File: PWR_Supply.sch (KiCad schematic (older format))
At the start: 0 parts

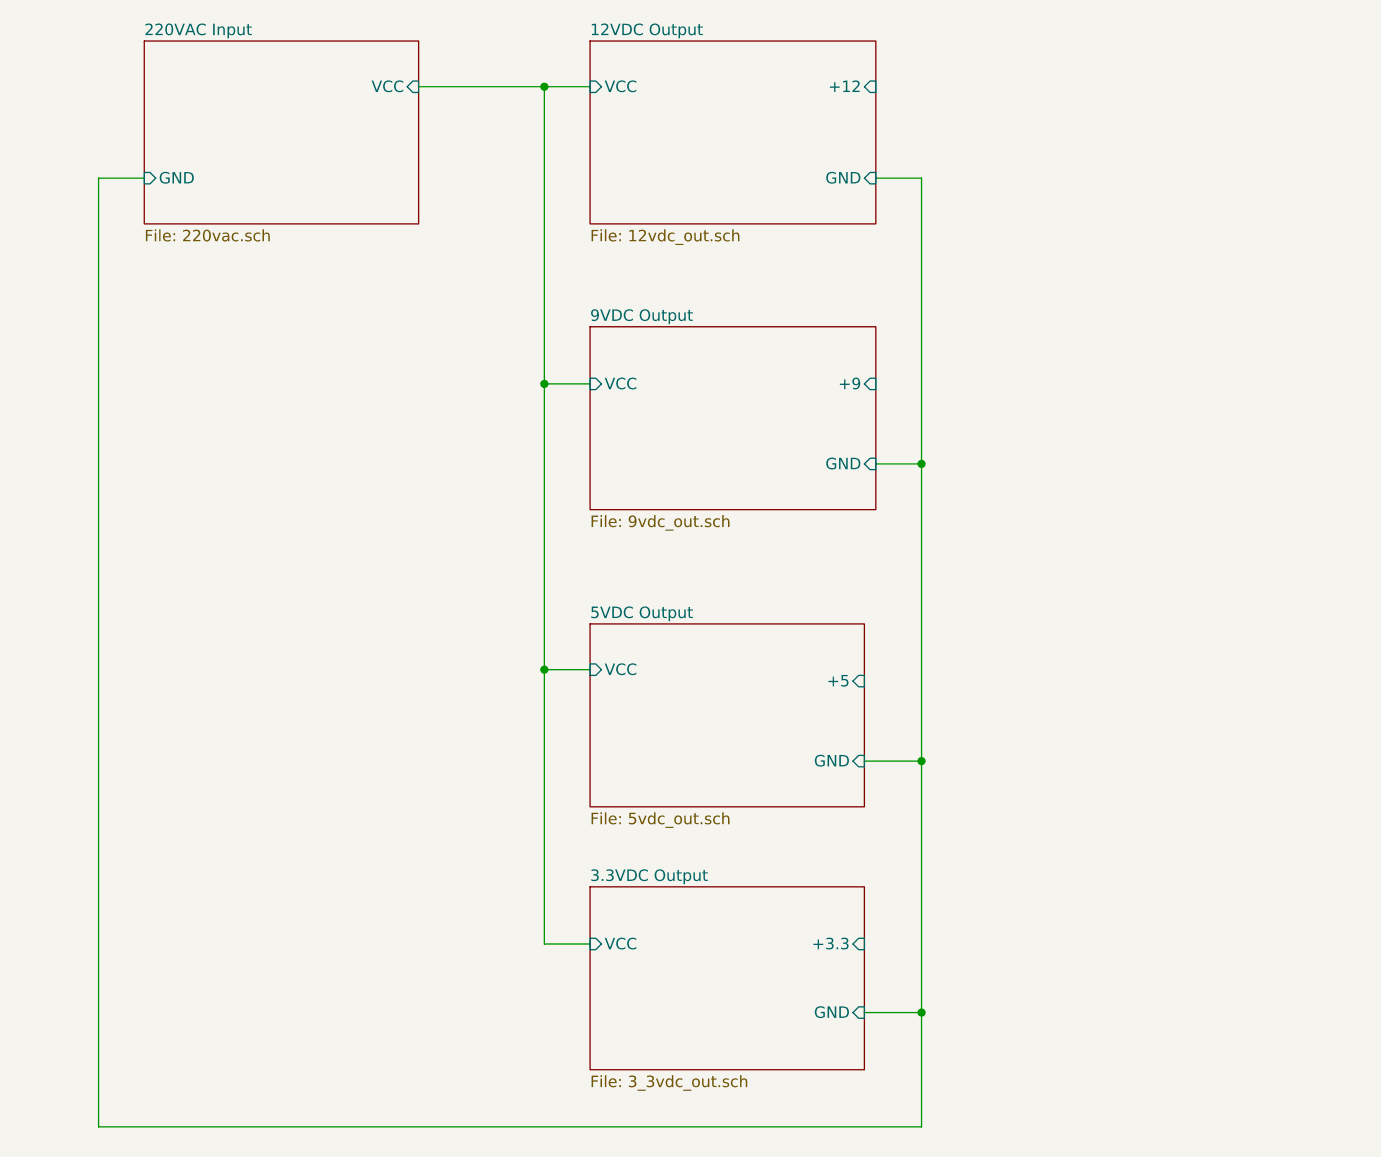
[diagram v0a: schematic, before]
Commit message: Fixed ERC errors, combined all outputs into a bus, fixed annotations
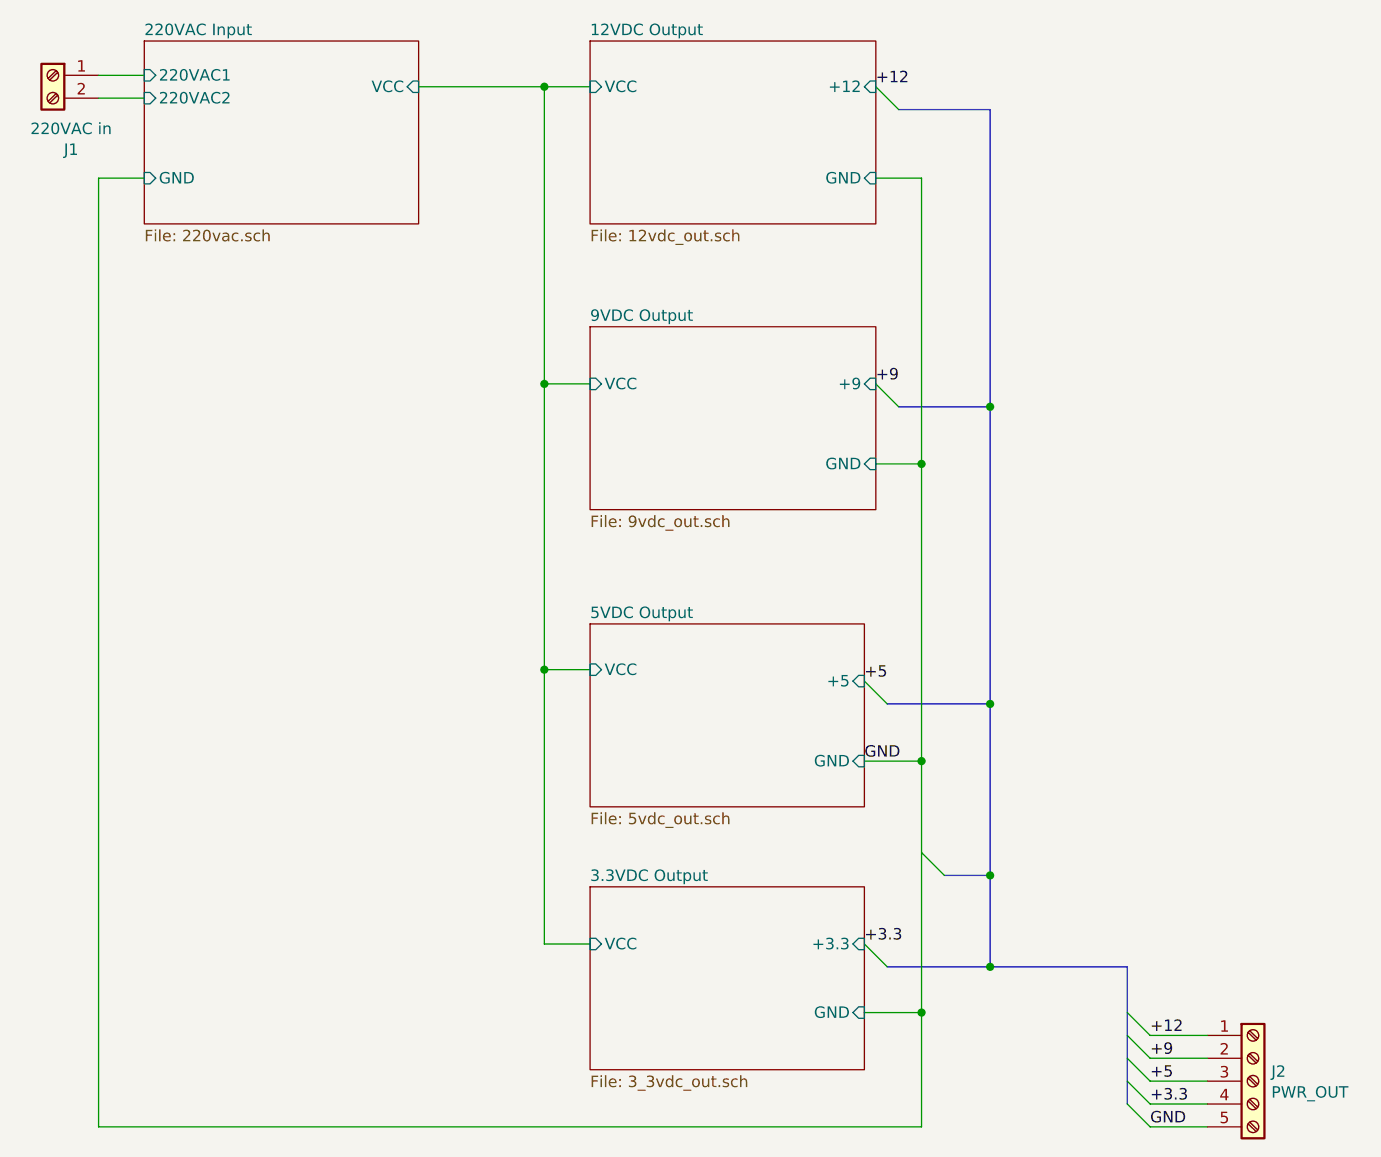
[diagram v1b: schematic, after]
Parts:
- added J1: 220VAC in, symbol Connector:Screw_Terminal_01x02
- added J2: PWR_OUT, symbol Connector:Screw_Terminal_01x05
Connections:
- new net +12: J2.1 (Pin_1)
- new net +3.3: J2.4 (Pin_4)
- new net +5: J2.3 (Pin_3)
- new net +9: J2.2 (Pin_2)
- new net 220VAC Input/220VAC1: J1.1 (Pin_1)
- new net 220VAC Input/220VAC2: J1.2 (Pin_2)
- new net GND: J2.5 (Pin_5)
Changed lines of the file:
@@
 encoding utf-8
 Sheet 1 6
-Title ""
-Date ""
+Title "Regulated power supply"
+Date "2020-03-18"
 Rev ""
 Comp ""
@@
 F2 "VCC" I R 3750 1850 50
 F3 "GND" I L 2550 2250 50
+F4 "220VAC1" I L 2550 1800 50
+F5 "220VAC2" I L 2550 1900 50
 $EndSheet
 $Sheet
@@
 	2350 6400 2350 2250
 Wire Wire Line
-	2350 2250 2550 2250
-Wire Wire Line
 	5750 3500 5950 3500
 Connection ~ 5950 3500
@@
 Connection ~ 5950 4800
 Wire Wire Line
-	5950 4800 5950 5900
-Wire Wire Line
 	5700 5900 5950 5900
 Connection ~ 5950 5900
 Wire Wire Line
 	5950 5900 5950 6400
+$Comp
+L Connector:Screw_Terminal_01x02 J?
+U 1 1 5E71DD55
+P 2150 1800
+AR Path="/5E6890B5/5E71DD55" Ref="J?"  Part="1"
+AR Path="/5E71DD55" Ref="J1"  Part="1"
+F 0 "J1" H 2070 1475 50  0000 C CNN
+F 1 "220VAC in" H 2070 1566 50  0000 C CNN
+F 2 "" H 2150 1800 50  0001 C CNN
+F 3 "~" H 2150 1800 50  0001 C CNN
+	1    2150 1800
+	-1   0    0    -1
+$EndComp
+Wire Wire Line
+	2350 1800 2550 1800
+Wire Wire Line
+	2550 1900 2350 1900
+$Comp
+L Connector:Screw_Terminal_01x05 J2
+U 1 1 5E71FE95
+P 7400 6200
+F 0 "J2" H 7480 6242 50  0000 L CNN
+F 1 "PWR_OUT" H 7480 6151 50  0000 L CNN
+F 2 "" H 7400 6200 50  0001 C CNN
+F 3 "~" H 7400 6200 50  0001 C CNN
+	1    7400 6200
+	1    0    0    -1
+$EndComp
+Entry Wire Line
+	6850 5900 6950 6000
+Entry Wire Line
+	6850 6000 6950 6100
+Entry Wire Line
+	6850 6100 6950 6200
+Entry Wire Line
+	6850 6200 6950 6300
+Entry Wire Line
+	6850 6300 6950 6400
+Text Label 6950 6000 0    50   ~ 0
++12
+Text Label 6950 6100 0    50   ~ 0
++9
+Text Label 6950 6200 0    50   ~ 0
++5
+Text Label 6950 6300 0    50   ~ 0
++3.3
+Text Label 6950 6400 0    50   ~ 0
+GND
+Wire Bus Line
+	6850 5700 6250 5700
+Entry Wire Line
+	5750 1850 5850 1950
+Entry Wire Line
+	5750 3150 5850 3250
+Entry Wire Line
+	5700 4450 5800 4550
+Entry Wire Line
+	5700 5600 5800 5700
+Wire Bus Line
+	5800 4550 6250 4550
+Connection ~ 6250 4550
+Wire Bus Line
+	6250 4550 6250 3250
+Wire Bus Line
+	5850 3250 6250 3250
+Connection ~ 6250 3250
+Wire Bus Line
+	6250 3250 6250 1950
+Wire Bus Line
+	5850 1950 6250 1950
+Wire Bus Line
+	6250 4550 6250 5300
+Wire Bus Line
+	6250 5700 5800 5700
+Connection ~ 6250 5700
+Entry Wire Line
+	5950 5200 6050 5300
+Wire Bus Line
+	6050 5300 6250 5300
+Connection ~ 6250 5300
+Wire Bus Line
+	6250 5300 6250 5700
+Text Label 5700 5600 0    50   ~ 0
++3.3
+Text Label 5700 4450 0    50   ~ 0
++5
+Text Label 5750 3150 0    50   ~ 0
++9
+Text Label 5750 1850 0    50   ~ 0
++12
+Text Label 5700 4800 0    50   ~ 0
+GND
+Wire Wire Line
+	7200 6000 6950 6000
+Wire Wire Line
+	6950 6100 7200 6100
+Wire Wire Line
+	7200 6200 6950 6200
+Wire Wire Line
+	6950 6300 7200 6300
+Wire Wire Line
+	7200 6400 6950 6400
+Wire Wire Line
+	2350 2250 2550 2250
+Wire Wire Line
+	5950 4800 5950 5900
+Wire Bus Line
+	6850 5700 6850 6300
 $EndSCHEMATC
